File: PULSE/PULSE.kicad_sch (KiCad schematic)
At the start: 17 parts, among them M1 Motor_Servo, M2 Motor_Servo, M3 Motor_Servo, M4 Motor_Servo, M5 Motor_Servo, M6 Motor_Servo, M7 Motor_Servo, M8 Motor_Servo, U1 Teensy4.1, U2 U1, U3 U2, U4 U3

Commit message: rotated
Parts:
- removed U6: ~, symbol lerdge_heatbed:lerdge_heatbed
- added U5: ~, symbol lerdge_heatbed:lerdge_heatbed
- renumbered U5 to U4
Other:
- moved on the sheet: U4
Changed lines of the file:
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@@
 		(on_board yes)
 		(dnp no)
-		(property "Reference" "U5"
-			(at 58.674 234.95 0)
+		(property "Reference" "U4"
+			(at 58.674 226.314 0)
 			(effects
 				(font
@@
 		(property "Description" ""
 			(at 59.69 228.6 0)
+			(effects
+				(font
+					(size 1.27 1.27)
+				)
+				(hide yes)
+			)
+		)
+		(pin ""
+		)
+		(pin ""
+		)
+		(pin ""
+		)
+		(pin ""
+		)
+		(pin ""
+		)
+		(pin ""
+		)
+		(instances
+			(project ""
+				(path "/2ccb6803-f597-4b91-b781-68e055fdefb5"
+					(reference "U4")
+					(unit 1)
+				)
+			)
+		)
+	)
+	(symbol
+		(lib_name "lerdge_heatbed_2")
+		(lib_id "lerdge_heatbed:lerdge_heatbed")
+		(at 91.44 228.6 0)
+		(unit 1)
+		(exclude_from_sim no)
+		(in_bom yes)
+		(on_board yes)
+		(dnp no)
+		(property "Reference" "U5"
+			(at 93.218 227.076 0)
+			(effects
+				(font
+					(size 1.27 1.27)
+				)
+				(justify right)
+			)
+		)
+		(property "Value" "~"
+			(at 82.55 247.0149 0)
+			(effects
+				(font
+					(size 1.27 1.27)
+				)
+				(justify right)
+			)
+		)
+		(property "Footprint" ""
+			(at 91.44 228.6 0)
+			(effects
+				(font
+					(size 1.27 1.27)
+				)
+				(hide yes)
+			)
+		)
+		(property "Datasheet" ""
+			(at 91.44 228.6 0)
+			(effects
+				(font
+					(size 1.27 1.27)
+				)
+				(hide yes)
+			)
+		)
+		(property "Description" ""
+			(at 91.44 228.6 0)
 			(effects
 				(font
@@
 					(unit 1)
 				)
-			)
-		)
-	)
-	(symbol
-		(lib_name "lerdge_heatbed_1")
-		(lib_id "lerdge_heatbed:lerdge_heatbed")
-		(at 105.41 228.6 0)
-		(unit 1)
-		(exclude_from_sim no)
-		(in_bom yes)
-		(on_board yes)
-		(dnp no)
-		(property "Reference" "U6"
-			(at 104.648 234.442 0)
-			(effects
-				(font
-					(size 1.27 1.27)
-				)
-				(justify left)
-			)
-		)
-		(property "Value" "~"
-			(at 118.11 245.7449 0)
-			(effects
-				(font
-					(size 1.27 1.27)
-				)
-				(justify left)
-			)
-		)
-		(property "Footprint" ""
-			(at 105.41 228.6 0)
-			(effects
-				(font
-					(size 1.27 1.27)
-				)
-				(hide yes)
-			)
-		)
-		(property "Datasheet" ""
-			(at 105.41 228.6 0)
-			(effects
-				(font
-					(size 1.27 1.27)
-				)
-				(hide yes)
-			)
-		)
-		(property "Description" ""
-			(at 105.41 228.6 0)
-			(effects
-				(font
-					(size 1.27 1.27)
-				)
-				(hide yes)
-			)
-		)
-		(pin ""
-		)
-		(pin ""
-		)
-		(pin ""
-		)
-		(pin ""
-		)
-		(pin ""
-		)
-		(pin ""
-		)
-		(instances
-			(project "PULSE"
-				(path "/2ccb6803-f597-4b91-b781-68e055fdefb5"
-					(reference "U6")
-					(unit 1)
-				)

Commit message: Finished up small transistor schematic
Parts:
- added Q1: 2N2219, Package_TO_SOT_THT:TO-39-3, symbol Transistor_BJT:2N2219
- added R1: 220 Ω, symbol Device:R_US
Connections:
- net GND: now also U4. (CONTROL-), U5. (CONTROL-)
- net Transistor Drain: now reaches U4. (CONTROL-)
- net Transistor Drain: now also U5. (CONTROL-), Q1.1 (E)
- net Transistor Gate: now reaches U1.20 (28_RX7)
- net Transistor Gate: now also R1.1
- new net: Q1.2 (B), R1.2
- new net VCC: Q1.3 (C)
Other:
- moved on the sheet: U5

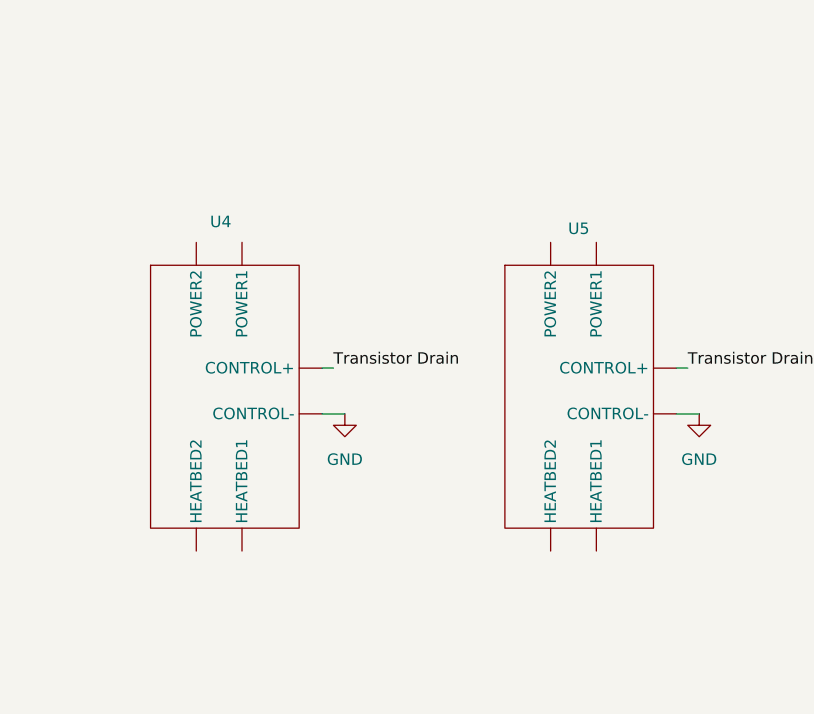
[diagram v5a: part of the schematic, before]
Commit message: Added solenoids
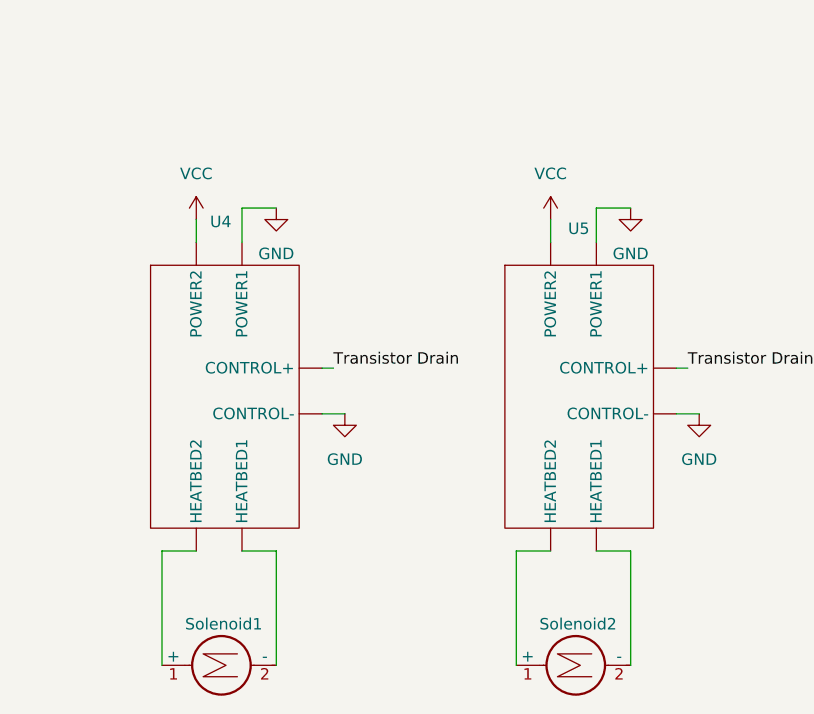
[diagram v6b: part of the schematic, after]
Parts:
- added Solenoid1, Solenoid2: ~, symbol Motor:Motor_DC
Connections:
- net VCC: now also U4. (CONTROL-), U5. (CONTROL-)
- new net: Solenoid1.1 (+), U4. (CONTROL-)
- new net: Solenoid1.2 (-), U4. (CONTROL-)
- new net: Solenoid2.1 (+), U5. (CONTROL-)
- new net: Solenoid2.2 (-), U5. (CONTROL-)
